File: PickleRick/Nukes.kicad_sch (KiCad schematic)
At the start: 47 parts, among them J10 Conn_01x03_Male, J11 Conn_01x03_Male, J12 Conn_01x03_Male, J13 Conn_01x03_Male, J6 Screw_Terminal_01x02, J7 Screw_Terminal_01x02, J8 Screw_Terminal_01x02, J9 Screw_Terminal_01x02, Q3 PMV20ENR, Q4 PMV20ENR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

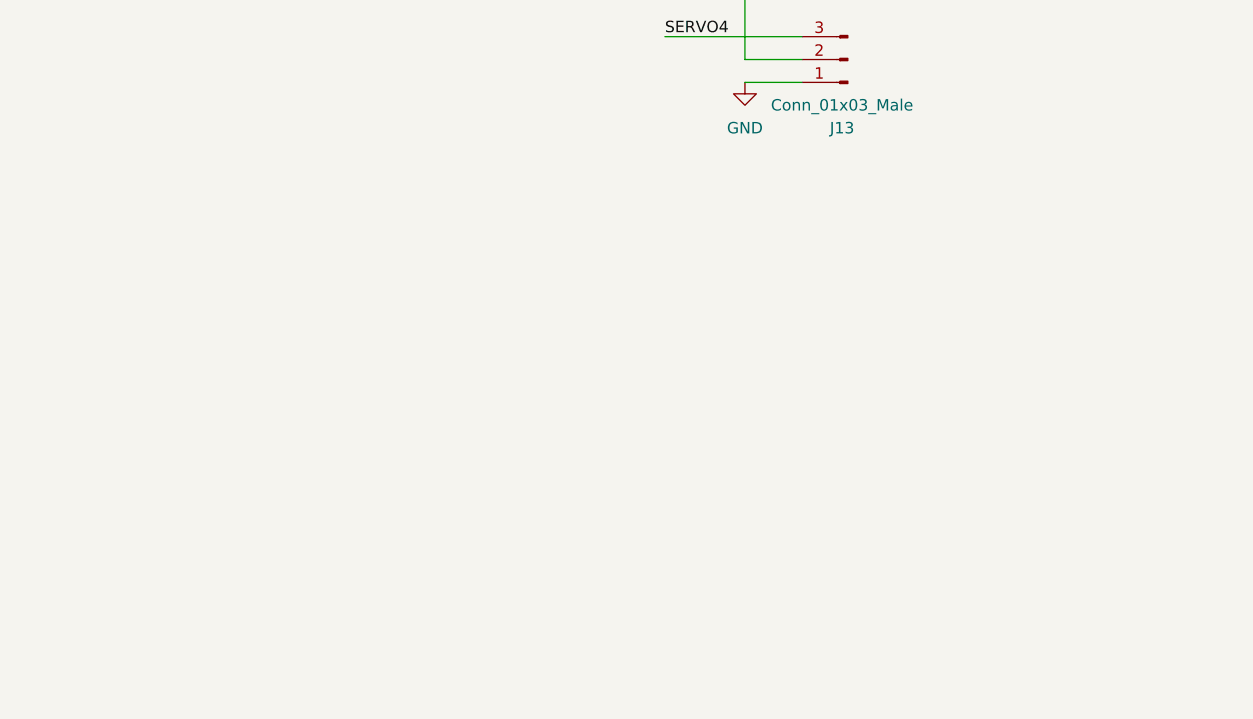
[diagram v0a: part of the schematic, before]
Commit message: Added LMR14050 buck converter to pickle rick
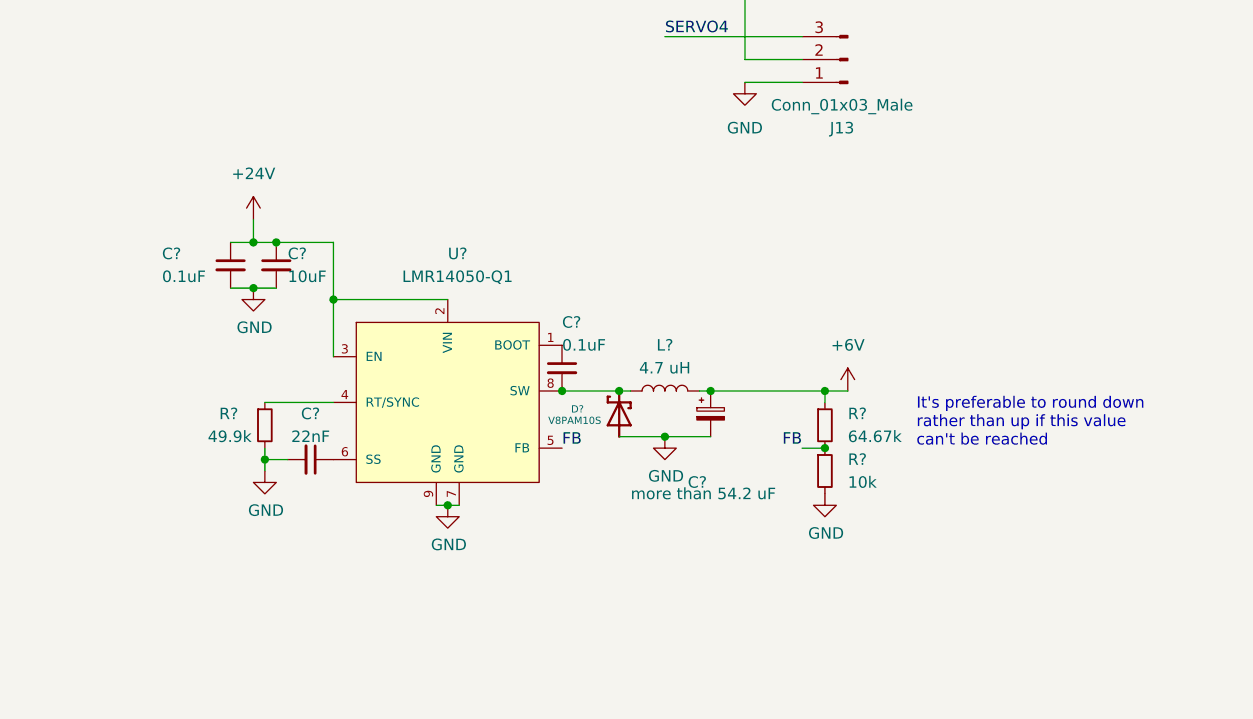
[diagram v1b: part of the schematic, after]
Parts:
- added C?: 22nF, symbol Device:C_Small
- added C?: 10uF, symbol Device:C_Small
- added C? (x2): 0.1uF, symbol Device:C_Small
- added C?: more than 54.2 uF, symbol Device:C_Polarized_Small
- added D?: V8PAM10S, DIO_V3PAN50-M3/I, symbol iclr:V8PAM10S
- added L?: 4.7 uH, symbol Device:L
- added R?: 64.67k, symbol Device:R_Small
- added R?: 49.9k, symbol Device:R_Small
- added R?: 10k, symbol Device:R_Small
- added U?: LMR14050-Q1, iclr:SOIC127P600X170-9N, symbol iclr:LMR14050-Q1
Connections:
- net +24V: now also C?.1, C?.1, U?.2 (VIN), U?.3 (EN)
- net +6V: now also C?.1, L?.2, R?.1
- net GND: now also C?.2, C?.2, C?.2, C?.2, D?.A, R?.2, R?.2, U?.7 (GND), U?.9 (GND)
- new net: C?.1, U?.6 (SS)
- new net: C?.2, D?.C, L?.1, U?.8 (SW)
- new net: R?.1, U?.4 (RT/SYNC)
- new net: C?.1, U?.1 (BOOT)
- new net FB: R?.1, R?.2, U?.5 (FB)
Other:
- note added: "It's preferable to round down rather than up if this value can't be reached"

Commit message: first full layout of pickle complete
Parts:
- removed C?: 22nF, symbol Device:C_Small
- removed C?: 10uF, symbol Device:C_Small
- removed C? (x2): 0.1uF, symbol Device:C_Small
- removed C?: more than 54.2 uF, symbol Device:C_Polarized_Small
- removed D13, D14, D7, D9: FIRING, LED_SMD:LED_0603_1608Metric, symbol Device:LED
- removed D?: V8PAM10S, DIO_V3PAN50-M3/I, symbol iclr:V8PAM10S
- removed J10, J11, J12, J13: Conn_01x03_Male, Connector_PinHeader_2.54mm:PinHeader_1x03_P2.54mm_Vertical, symbol Connector:Conn_01x03_Male
- removed J6, J7, J8, J9: Screw_Terminal_01x02, iclr-hw:PHOENIX_1757242, symbol Connector:Screw_Terminal_01x02
- removed L?: 4.7 uH, symbol Device:L
- removed Q3, Q4, Q5, Q6: PMV20ENR, Package_TO_SOT_SMD:SOT-23, symbol Device:Q_NMOS_GSD
- removed R23, R24, R31, R32: 2K, Resistor_SMD:R_0603_1608Metric, symbol Device:R
- removed R?: 64.67k, symbol Device:R_Small
- removed R?: 49.9k, symbol Device:R_Small
- removed R?: 10k, symbol Device:R_Small
- removed U?: LMR14050-Q1, iclr:SOIC127P600X170-9N, symbol iclr:LMR14050-Q1
- added J12: Conn_01x05_Male, Connector_PinHeader_2.54mm:PinHeader_1x05_P2.54mm_Vertical, symbol Connector:Conn_01x05_Male
- added J6: Screw_Terminal_01x08, TerminalBlock_TE-Connectivity:TerminalBlock_TE_282834-8_1x08_P2.54mm_Horizontal, symbol Connector:Screw_Terminal_01x08
- added Q3, Q4, Q5, Q6: NCV8415STT1G, Package_TO_SOT_SMD:SOT-223, symbol Driver_FET:NCV8402xST
- D10, D15, D16, D8: footprint Diode_SMD:D_SOD-123F -> Diode_SMD:D_SOD-128
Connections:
- net +24V: now also J6.2 (Pin_2), J6.4 (Pin_4), J6.6 (Pin_6), J6.8 (Pin_8)
- net Cont1: now also U4.10, U5.9 (P6); no longer U4.16, U5.2 (P0)
- net Cont2: now also U4.12, U5.7 (P4); no longer U4.14, U5.4 (P2)
- net Cont3: now also U4.14, U5.4 (P2); no longer U4.12, U5.7 (P4)
- net Cont4: now also U4.16, U5.2 (P0); no longer U4.10, U5.9 (P6)
- net GND: now also C7.2, C8.2, U6.11 (VSS), U6.29 (VSS), J12.1 (Pin_1), Q3.3 (S), Q4.3 (S), Q5.3 (S), Q6.3 (S)
- net Nuke1: now also U5.10 (P7), Q3.1 (G); no longer U5.3 (P1)
- net Nuke2: now also U5.8 (P5), Q5.1 (G); no longer U5.5 (P3)
- net Nuke3: now also U5.5 (P3), Q4.1 (G); no longer U5.8 (P5)
- net Nuke4: now also U5.3 (P1), Q6.1 (G); no longer U5.10 (P7)
- net SERVO1: now also U6.10 (LED7), J12.2 (Pin_2); no longer U6.3 (LED0)
- net SERVO2: now also U6.12 (LED8), J12.3 (Pin_3); no longer U6.4 (LED1)
- net SERVO3: now also U6.13 (LED9), J12.4 (Pin_4); no longer U6.5 (LED2)
- net SERVO4: now also U6.14 (LED10), J12.5 (Pin_5); no longer U6.6 (LED3)
- net Nuke1-: now reaches D11.2 (A), D8.2 (A)
- net Nuke1-: now also U4.8, J6.7 (Pin_7); no longer U4.2
- net at R36.1: now also U4.1; no longer U4.7
- net Nuke4-: now reaches D16.2 (A), D18.2 (A)
- net Nuke4-: now also U4.2, J6.1 (Pin_1); no longer U4.8
- net Nuke3-: now reaches D10.2 (A), D12.2 (A)
- net Nuke3-: now also U4.4, J6.3 (Pin_3); no longer U4.6
- net at D16.1 (K): now also Q6.2 (D), Q6.4 (D)
- net at R27.1: now also U4.7; no longer U4.1
- net Nuke2-: now reaches D15.2 (A), D17.2 (A)
- net Nuke2-: now also U4.6, J6.5 (Pin_5); no longer U4.4
- net at D8.1 (K): now also Q3.2 (D), Q3.4 (D)
- net at D10.1 (K): now also Q4.2 (D), Q4.4 (D)
- net at D15.1 (K): now also Q5.2 (D), Q5.4 (D)
- net at U4.3: now also R29.1; no longer R35.1
- net at U4.5: now also R35.1; no longer R29.1
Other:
- note removed: "It's preferable to round down rather than up if this value can't be reached"
- moved on the sheet: D10, D11, D12, D15, D16, D17, D18, D8, R25, R26, R27, R28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

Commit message: pickle layed out
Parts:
- removed D11, D12, D17, D18: CONTINUITY, LED_SMD:LED_0603_1608Metric, symbol Device:LED
- removed R28, R30, R37, R38: 2K, Resistor_SMD:R_0603_1608Metric, symbol Device:R
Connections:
- net +3V3: now also U4.10, U4.12, U4.14, U4.16; no longer U4.11, U4.13, U4.15, U4.9
- net Cont1: now also U4.9; no longer U4.10
- net Cont2: now also U4.11; no longer U4.12
- net Cont3: now also U4.13; no longer U4.14
- net Cont4: now also U4.15; no longer U4.16
- net Nuke1-: now also U4.7; no longer U4.8
- net Nuke2-: now also U4.5; no longer U4.6
- net Nuke3-: now also U4.3; no longer U4.4
- net Nuke4-: now also U4.1; no longer U4.2
- net at R36.1: now also U4.2; no longer U4.1
- net at R29.1: now also U4.4; no longer U4.3
- net at R35.1: now also U4.6; no longer U4.5
- net at R27.1: now also U4.8; no longer U4.7
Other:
- moved on the sheet: U4A, U4B, U4C, U4D
